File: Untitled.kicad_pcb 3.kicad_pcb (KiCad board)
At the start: 2 copper layers, 37 x 37 mm, 22 parts, among them J1 Battery Connector, J2 Top Screw Terminal, J3 Bottom Screw Terminal, Q1 Q_NMOS_DGS, Q2 Q_NMOS_DGS, Q3 Q_NMOS_DGS, U1 XIAO-ESP32-S3-SMD, U3 LSM6DSO32, U4 MS5611-01BA

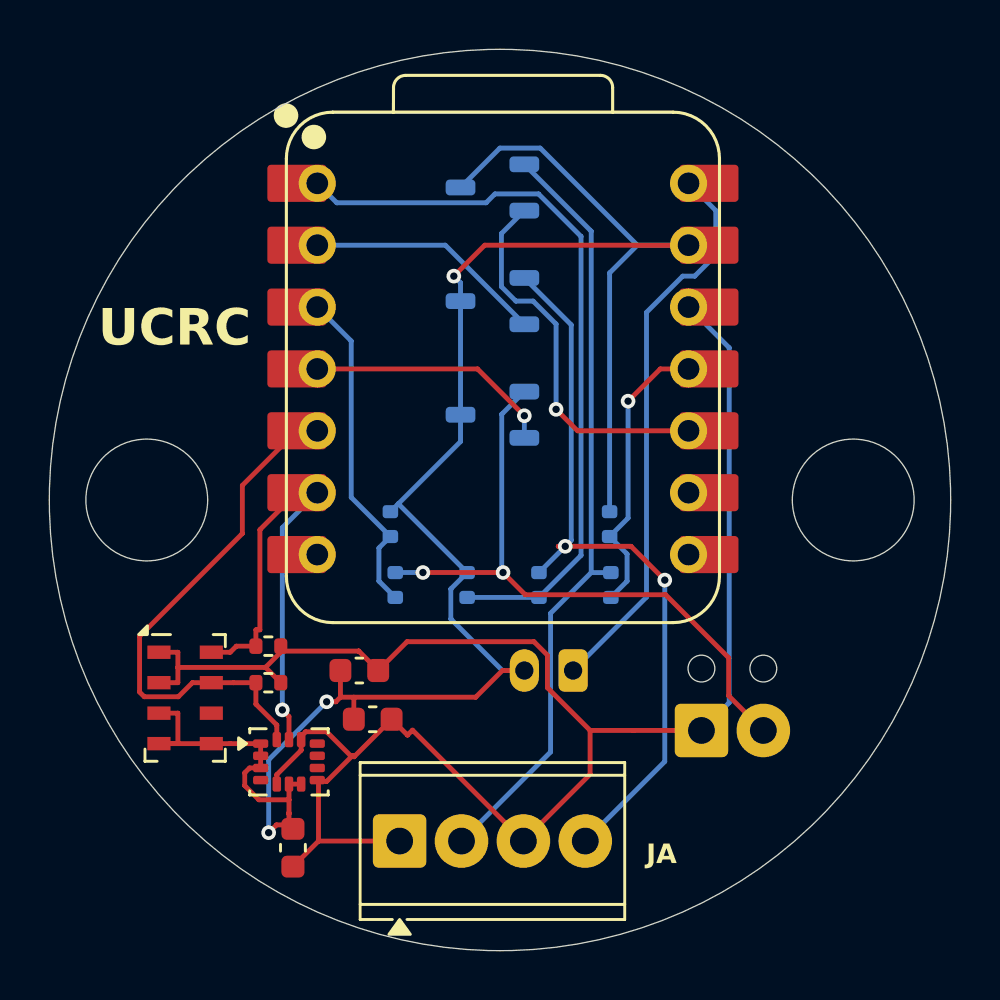
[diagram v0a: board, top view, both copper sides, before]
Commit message: My PCB design
I arranged the parts and then used an automatic routing thingy to attach all of the nodes. I then made sure it followed the design rules checker and that's it.
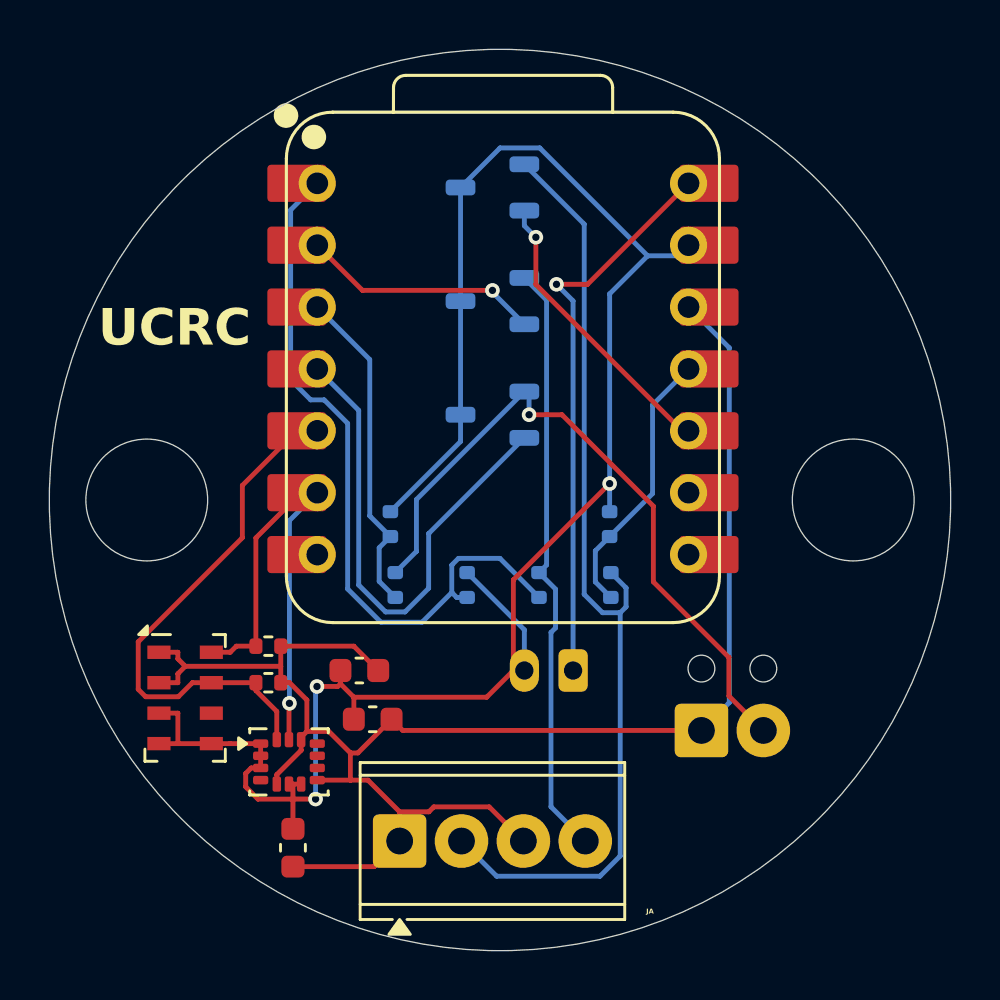
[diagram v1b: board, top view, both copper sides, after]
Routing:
- net /IGNIT 3: track 11.0 -> 21.9 mm, vias 1 -> 0
- net /APPO: track 31.9 -> 39.9 mm
- net /MAIN: track 31.3 -> 24.6 mm, vias 2 -> 0
- net +3.3V: track 77.9 -> 71.7 mm
- net -BATT: track 86.9 -> 82.0 mm
- net /IGNIT 1: track 16.5 -> 12.8 mm
- net /MOTOR: track 26.8 -> 28.4 mm, vias 2 -> 1
- net /CONT 1: track 12.8 -> 12.1 mm, vias 1 -> 0
- net /CONT 2: track 31.4 -> 30.8 mm
- net +BATT: track 24.0 -> 24.1 mm, vias 0 -> 1
- net /IGNIT 2: vias 0 -> 1
